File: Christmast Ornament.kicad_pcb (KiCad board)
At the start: 2 copper layers, 98.8 x 98.7 mm, 63 parts, among them J1 USB_OTG, J2 CONN_01X06, Q1 8205A, Q2 SI2302, Q3 BC817, SW1 SW_Push, SW2 SW_Push, U1 TP4056, U10 WS2812b, U2 HT7833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

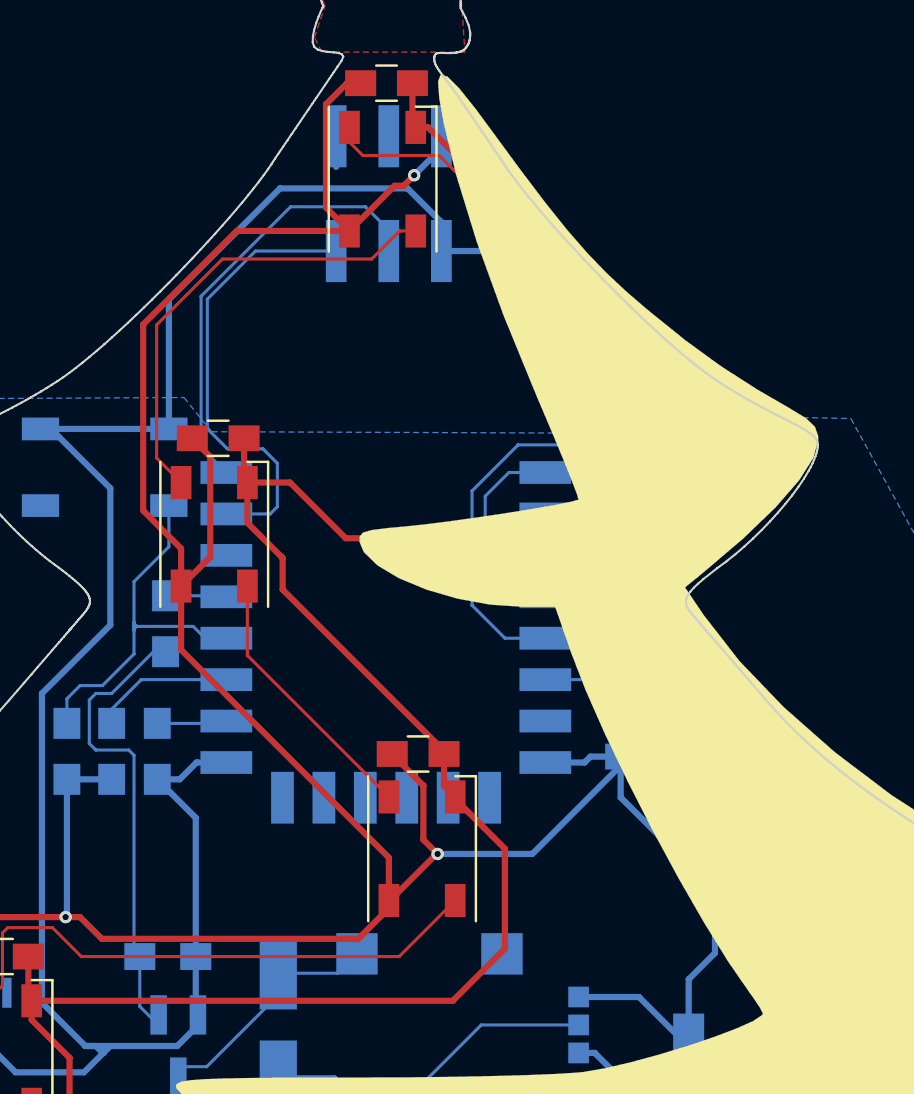
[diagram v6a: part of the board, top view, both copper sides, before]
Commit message: capInput routed and R12 deleted
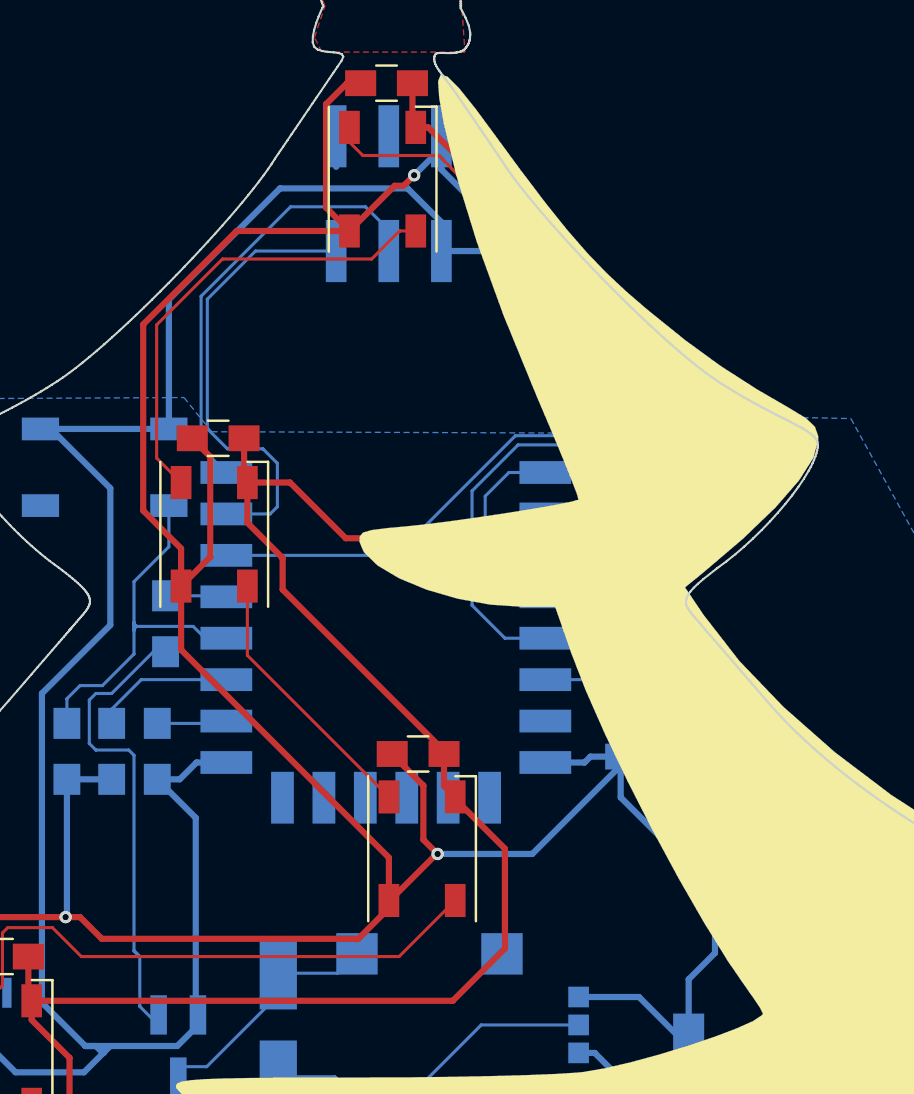
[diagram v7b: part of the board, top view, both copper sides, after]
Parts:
- removed R12: 10K, Resistors_SMD:R_0805_HandSoldering
- moved C13 3.60 mm to (182.5, 67.3)
- moved R14 3.21 mm to (180.1, 65.2), turned to 180 degrees
- moved D5 0.54 mm to (185.7, 68.7)
- moved Q2 0.19 mm to (179.7, 75.8)
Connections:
- C13 pad 1: Net-(C13-Pad1) -> /capInput
- D5 pad 2: Net-(C13-Pad1) -> /capInput
- R14 pad 2: Net-(C13-Pad1) -> /capInput
- U4 pad 20: Net-(U4-Pad20) -> /capInput
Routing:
- net /capInput: track 0.00 -> 31.1 mm, vias 0 -> 2
- net Net-(C13-Pad1): track 6.30 -> 0.00 mm
- net GND: track 324.9 -> 326.7 mm
- net /PIX_DATA: track 38.8 -> 37.3 mm
- net +3V3: track 285.6 -> 286.5 mm
- net Net-(D4-Pad1): track 117.8 -> 117.2 mm

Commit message: SSID and password added to back silkscreen
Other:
- board text added: "SSID: Arbolito Passw: qwerty"
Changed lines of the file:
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@@
     (links 122)
     (no_connects 4)
-    (area 107.9065 37.751949 229.191501 146.367501)
+    (area 118.662046 37.751949 217.545316 136.571691)
     (thickness 1.6)
-    (drawings 769)
+    (drawings 770)
     (tracks 544)
     (zones 0)
@@
   (layers
     (0 F.Cu signal)
-    (31 B.Cu signal)
+    (31 B.Cu signal hide)
     (32 B.Adhes user)
     (33 F.Adhes user)
@@
     (35 F.Paste user)
     (36 B.SilkS user)
-    (37 F.SilkS user)
+    (37 F.SilkS user hide)
     (38 B.Mask user)
     (39 F.Mask user)
@@
     )
   )
+  (gr_text "SSID: Arbolito\nPassw: qwerty" (at 168.041 89.281) (layer B.SilkS)
+    (effects (font (size 0.8 0.8) (thickness 0.15)) (justify mirror))
+  )
   (gr_text Rx (at 164.231 59.055) (layer B.SilkS)
